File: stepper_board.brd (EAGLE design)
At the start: 101.1 x 81.3 mm, 83 parts, among them IC1 MCP1703DB, U2 MIC2005A-1YM5, Y1 12 MHz

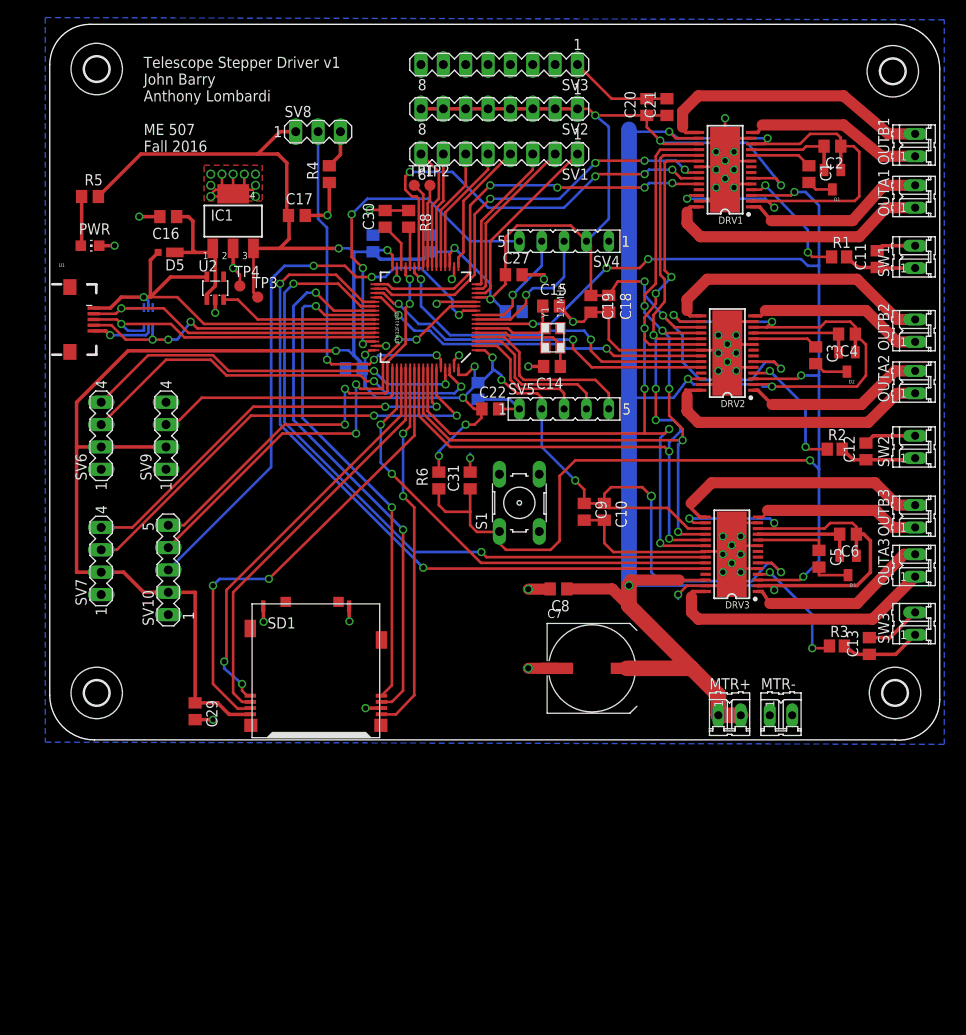
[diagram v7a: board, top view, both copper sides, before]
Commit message: Modified silkscreen layer to make labels clear
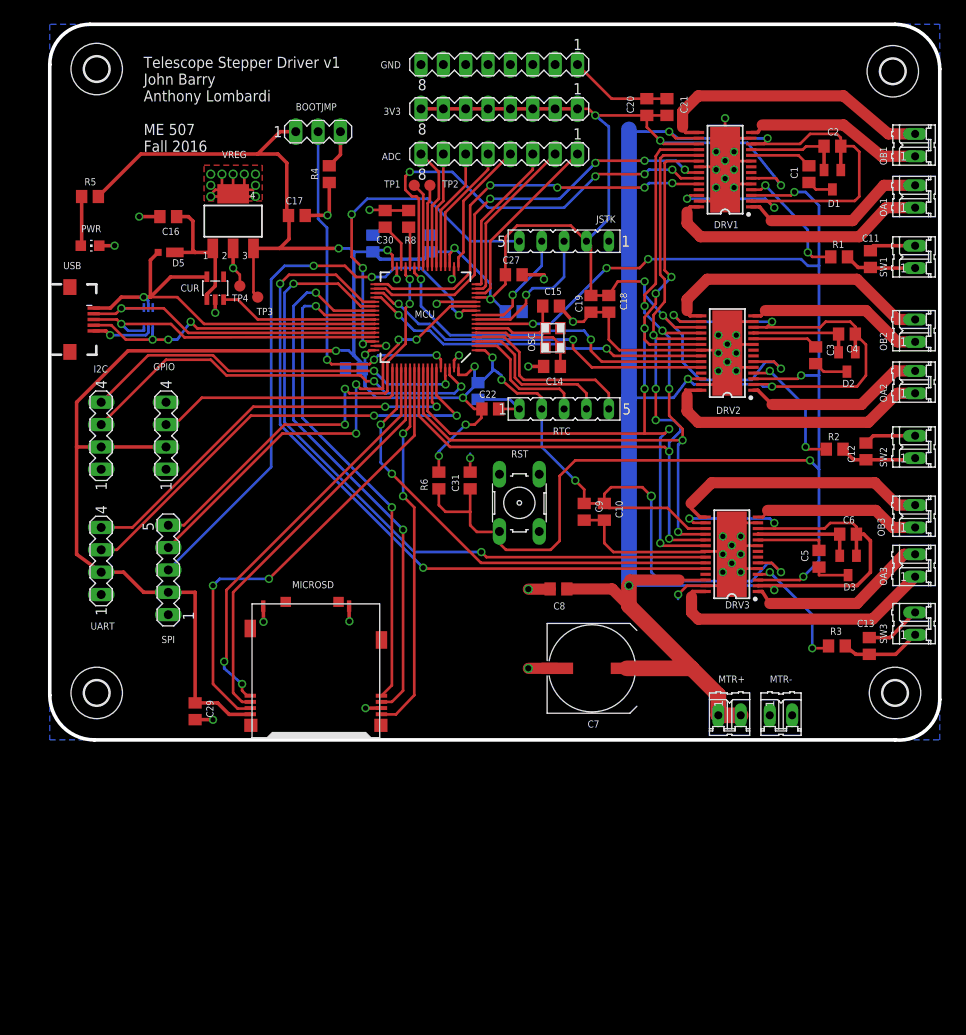
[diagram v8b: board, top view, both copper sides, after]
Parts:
- moved C11 0.76 mm to (92.7, 54.1)
- renumbered IC1 to VREG, OUTA1 to OA1, OUTA2 to OA2, OUTA3 to OA3, OUTB1 to OB1, OUTB2 to OB2, OUTB3 to OB3, S1 to RST, SD1 to MICROSD, STM32F411RE to MCU, SV1 to ADC, SV10 to SPI, SV2 to 3V3, SV3 to GND, SV4 to JSTK, SV5 to RTC, SV6 to I2C, SV7 to UART, SV8 to BOOTJMP, SV9 to GPIO, U$1 to ESD, U1 to USB, U2 to CUR, Y1 to OSC
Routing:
- net +3V3: track 449.9 -> 448.6 mm
- net GND: track 212.7 -> 213.5 mm
